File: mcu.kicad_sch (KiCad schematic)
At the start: 41 parts, among them SW1 SW_Nidec_CAS-120A1, SW2 CK_KMS2xxG, U1 STM32U5G9ZJTxQ, Y1 NX2016SA-16MHZ-EXS00A-CS07826, Y2 NX2012SA-32.768K-STD-MUB-1

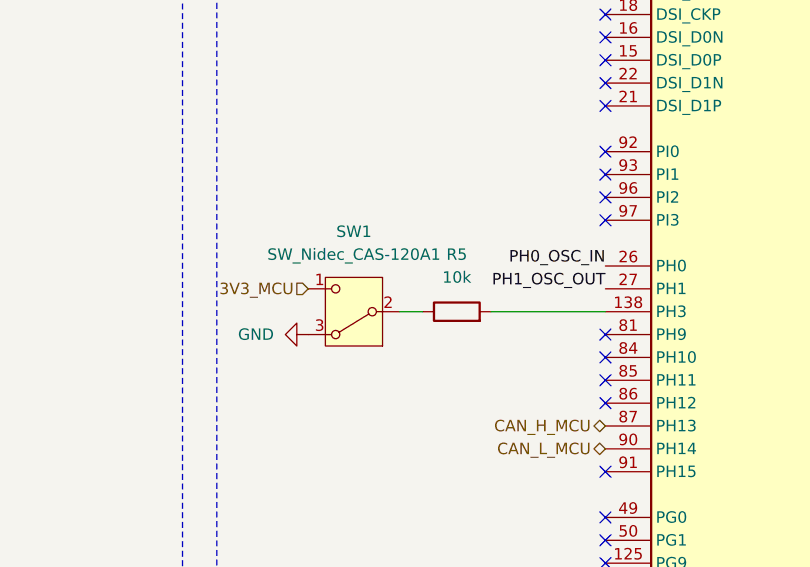
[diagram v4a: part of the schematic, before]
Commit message: Add switch reference form WE for boot selection mode
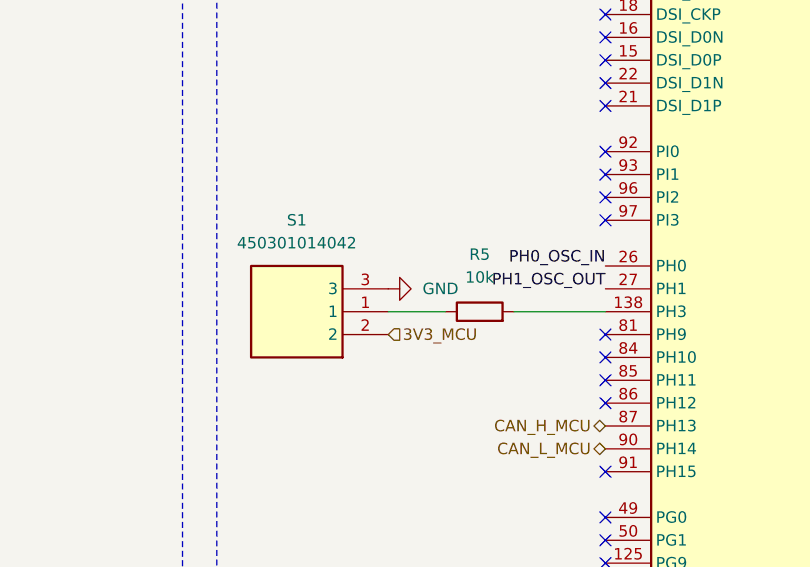
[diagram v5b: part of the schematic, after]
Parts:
- removed SW1: SW_Nidec_CAS-120A1, Button_Switch_SMD:Nidec_Copal_CAS-120A, symbol Switch:SW_Nidec_CAS-120A1
- added S1: 450301014042, weather-station-poc-fp:450301014042, symbol weather-station-poc-sym:450301014042
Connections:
- net 3V3_MCU: now also S1.2
- net GND: now also S1.3
- net at R5.1: now also S1.1
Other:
- moved on the sheet: R5
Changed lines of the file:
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@@
 	(wire
 		(pts
-			(xy 226.06 110.49) (xy 238.76 110.49)
+			(xy 228.6 110.49) (xy 238.76 110.49)
 		)
 		(stroke
@@
 	(wire
 		(pts
-			(xy 276.86 232.41) (xy 279.4 232.41)
+			(xy 220.98 110.49) (xy 214.63 110.49)
 		)
 		(stroke
@@
 	(wire
 		(pts
-			(xy 341.63 157.48) (xy 341.63 153.67)
+			(xy 276.86 232.41) (xy 279.4 232.41)
 		)
 		(stroke
@@
 	(wire
 		(pts
-			(xy 215.9 110.49) (xy 218.44 110.49)
+			(xy 341.63 157.48) (xy 341.63 153.67)
 		)
 		(stroke
@@
 	(hierarchical_label "3V3_MCU"
 		(shape input)
-		(at 205.74 107.95 180)
+		(at 214.63 113.03 0)
 		(effects
 			(font
 				(size 1.27 1.27)
 			)
-			(justify right)
+			(justify left)
 		)
 	)
@@
 	)
 	(symbol
-		(lib_id "power:GND")
-		(at 205.74 113.03 270)
-		(unit 1)
-		(exclude_from_sim no)
-		(in_bom yes)
-		(on_board yes)
-		(dnp no)
-		(fields_autoplaced yes)
-		(property "Reference" "#PWR054"
-			(at 199.39 113.03 0)
-			(effects
-				(font
-					(size 1.27 1.27)
-				)
-				(hide yes)
-			)
-		)
-		(property "Value" "GND"
-			(at 201.93 113.0299 90)
-			(effects
-				(font
-					(size 1.27 1.27)
-				)
-				(justify right)
-			)
-		)
-		(property "Footprint" ""
-			(at 205.74 113.03 0)
-			(effects
-				(font
-					(size 1.27 1.27)
-				)
-				(hide yes)
-			)
-		)
-		(property "Datasheet" ""
-			(at 205.74 113.03 0)
-			(effects
-				(font
-					(size 1.27 1.27)
-				)
-				(hide yes)
-			)
-		)
-		(property "Description" "Power symbol creates a global label with name \"GND\" , ground"
-			(at 205.74 113.03 0)
-			(effects
-				(font
-					(size 1.27 1.27)
-				)
-				(hide yes)
-			)
-		)
-		(pin "1"
-		)
-		(instances
-			(project "weather-station-poc"
-				(path "/38eb53bb-294e-46e4-ad59-fd355ca373b9/5f00b1ab-9f48-4782-8810-a8d68b4e6a2f"
-					(reference "#PWR054")
-					(unit 1)
-				)
-			)
-		)
-	)
-	(symbol
 		(lib_id "Device:C")
 		(at 81.28 90.17 0)
@@
 	(symbol
 		(lib_id "Device:R")
-		(at 222.25 110.49 90)
+		(at 224.79 110.49 90)
 		(unit 1)
 		(exclude_from_sim no)
@@
 		(fields_autoplaced yes)
 		(property "Reference" "R5"
-			(at 222.25 104.14 90)
+			(at 224.79 104.14 90)
 			(effects
 				(font
@@
 		)
 		(property "Value" "10k"
-			(at 222.25 106.68 90)
+			(at 224.79 106.68 90)
 			(effects
 				(font
@@
 		)
 		(property "Footprint" "Resistor_SMD:R_0603_1608Metric_Pad0.98x0.95mm_HandSolder"
-			(at 222.25 112.268 90)
+			(at 224.79 112.268 90)
 			(effects
 				(font
@@
 		)
 		(property "Datasheet" "~"
-			(at 222.25 110.49 0)
+			(at 224.79 110.49 0)
 			(effects
 				(font
@@
 		)
 		(property "Description" "Resistor"
-			(at 222.25 110.49 0)
+			(at 224.79 110.49 0)
 			(effects
 				(font
@@
 	)
 	(symbol
+		(lib_id "weather-station-poc-sym:450301014042")
+		(at 214.63 113.03 180)
+		(unit 1)
+		(exclude_from_sim no)
+		(in_bom yes)
+		(on_board yes)
+		(dnp no)
+		(fields_autoplaced yes)
+		(property "Reference" "S1"
+			(at 204.47 100.33 0)
+			(effects
+				(font
+					(size 1.27 1.27)
+				)
+			)
+		)
+		(property "Value" "450301014042"
+			(at 204.47 102.87 0)
+			(effects
+				(font
+					(size 1.27 1.27)
+				)
+			)
+		)
+		(property "Footprint" "weather-station-poc-fp:450301014042"
+			(at 198.12 18.11 0)
+			(effects
+				(font
+					(size 1.27 1.27)
+				)
+				(justify left top)
+				(hide yes)
+			)
+		)
+		(property "Datasheet" "https://www.we-online.com/catalog/datasheet/450301014042.pdf"
+			(at 198.12 -81.89 0)
+			(effects
+				(font
+					(size 1.27 1.27)
+				)
+				(justify left top)
+				(hide yes)
+			)
+		)
+		(property "Description" "WS-SLTV Mini Slide Switch 10mm*2.5mm. SPDT, ON-ON, 2.54mm, vertical type, THT, bulk"
+			(at 214.63 113.03 0)
+			(effects
+				(font
+					(size 1.27 1.27)
+				)
+				(hide yes)
+			)
+		)
+		(property "Height" ""
+			(at 198.12 -281.89 0)
+			(effects
+				(font
+					(size 1.27 1.27)
+				)
+				(justify left top)
+				(hide yes)
+			)
+		)
+		(property "Mouser Part Number" "710-450301014042"
+			(at 198.12 -381.89 0)
+			(effects
+				(font
+					(size 1.27 1.27)
+				)
+				(justify left top)
+				(hide yes)
+			)
+		)
+		(property "Mouser Price/Stock" "https://www.mouser.co.uk/ProductDetail/Wurth-Elektronik/450301014042?qs=wr8lucFkNMW0uepaR4R%2Fww%3D%3D"
+			(at 198.12 -481.89 0)
+			(effects
+				(font
+					(size 1.27 1.27)
+				)
+				(justify left top)
+				(hide yes)
+			)
+		)
+		(property "Manufacturer_Name" "Wurth Elektronik"
+			(at 198.12 -581.89 0)
+			(effects
+				(font
+					(size 1.27 1.27)
+				)
+				(justify left top)
+				(hide yes)
+			)
+		)
+		(property "Manufacturer_Part_Number" "450301014042"
+			(at 198.12 -681.89 0)
+			(effects
+				(font
+					(size 1.27 1.27)
+				)
+				(justify left top)
+				(hide yes)
+			)
+		)
+		(pin "2"
+		)
+		(pin "3"
+		)
+		(pin "1"
+		)
+		(instances
+			(project ""
+				(path "/38eb53bb-294e-46e4-ad59-fd355ca373b9/5f00b1ab-9f48-4782-8810-a8d68b4e6a2f"
+					(reference "S1")
+					(unit 1)
+				)
+			)
+		)
+	)
+	(symbol
 		(lib_id "Device:C")
 		(at 132.08 179.07 0)
@@
 	(symbol
 		(lib_id "power:GND")
+		(at 214.63 107.95 90)
+		(unit 1)
+		(exclude_from_sim no)
+		(in_bom yes)
+		(on_board yes)
+		(dnp no)
+		(fields_autoplaced yes)
+		(property "Reference" "#PWR0122"
+			(at 220.98 107.95 0)
+			(effects
+				(font
+					(size 1.27 1.27)
+				)
+				(hide yes)
+			)
+		)
+		(property "Value" "GND"
+			(at 218.44 107.9499 90)
+			(effects
+				(font
+					(size 1.27 1.27)
+				)
+				(justify right)
+			)
+		)
+		(property "Footprint" ""
+			(at 214.63 107.95 0)
+			(effects
+				(font
+					(size 1.27 1.27)
+				)
+				(hide yes)
+			)
+		)
+		(property "Datasheet" ""
+			(at 214.63 107.95 0)
+			(effects
+				(font
+					(size 1.27 1.27)
+				)
+				(hide yes)
+			)
+		)
+		(property "Description" "Power symbol creates a global label with name \"GND\" , ground"
+			(at 214.63 107.95 0)
+			(effects
+				(font
+					(size 1.27 1.27)
+				)
+				(hide yes)
+			)
+		)
+		(pin "1"
+		)
+		(instances
+			(project "weather-station-poc"
+				(path "/38eb53bb-294e-46e4-ad59-fd355ca373b9/5f00b1ab-9f48-4782-8810-a8d68b4e6a2f"
+					(reference "#PWR0122")
+					(unit 1)
+				)
+			)
+		)
+	)
+	(symbol
+		(lib_id "power:GND")
 		(at 100.33 207.01 0)
 		(unit 1)
@@
 					(unit 1)
 				)
-			)
-		)
-	)
-	(symbol
-		(lib_id "Switch:SW_Nidec_CAS-120A1")
-		(at 210.82 110.49 180)
-		(unit 1)
-		(exclude_from_sim no)
-		(in_bom yes)
-		(on_board yes)
-		(dnp no)
-		(fields_autoplaced yes)
-		(property "Reference" "SW1"
-			(at 210.82 101.6 0)
-			(effects
-				(font
-					(size 1.27 1.27)
-				)
-			)
-		)
-		(property "Value" "SW_Nidec_CAS-120A1"
-			(at 210.82 104.14 0)
-			(effects
-				(font
-					(size 1.27 1.27)
-				)
-			)
-		)
-		(property "Footprint" "Button_Switch_SMD:Nidec_Copal_CAS-120A"
-			(at 210.82 100.33 0)
-			(effects
-				(font
-					(size 1.27 1.27)
-				)
-				(hide yes)
-			)
-		)
-		(property "Datasheet" "https://www.nidec-components.com/e/catalog/switch/cas.pdf"
-			(at 210.82 102.87 0)
-			(effects
-				(font
-					(size 1.27 1.27)
-				)
-				(hide yes)
-			)
-		)
-		(property "Description" "Switch, single pole double throw"
-			(at 210.82 110.49 0)
-			(effects
-				(font
-					(size 1.27 1.27)
-				)
-				(hide yes)
-			)
-		)
-		(pin "2"
-		)
-		(pin "1"
-		)
-		(pin "3"
-		)
-		(instances
-			(project ""
-				(path "/38eb53bb-294e-46e4-ad59-fd355ca373b9/5f00b1ab-9f48-4782-8810-a8d68b4e6a2f"
-					(reference "SW1")
-					(unit 1)
-				)

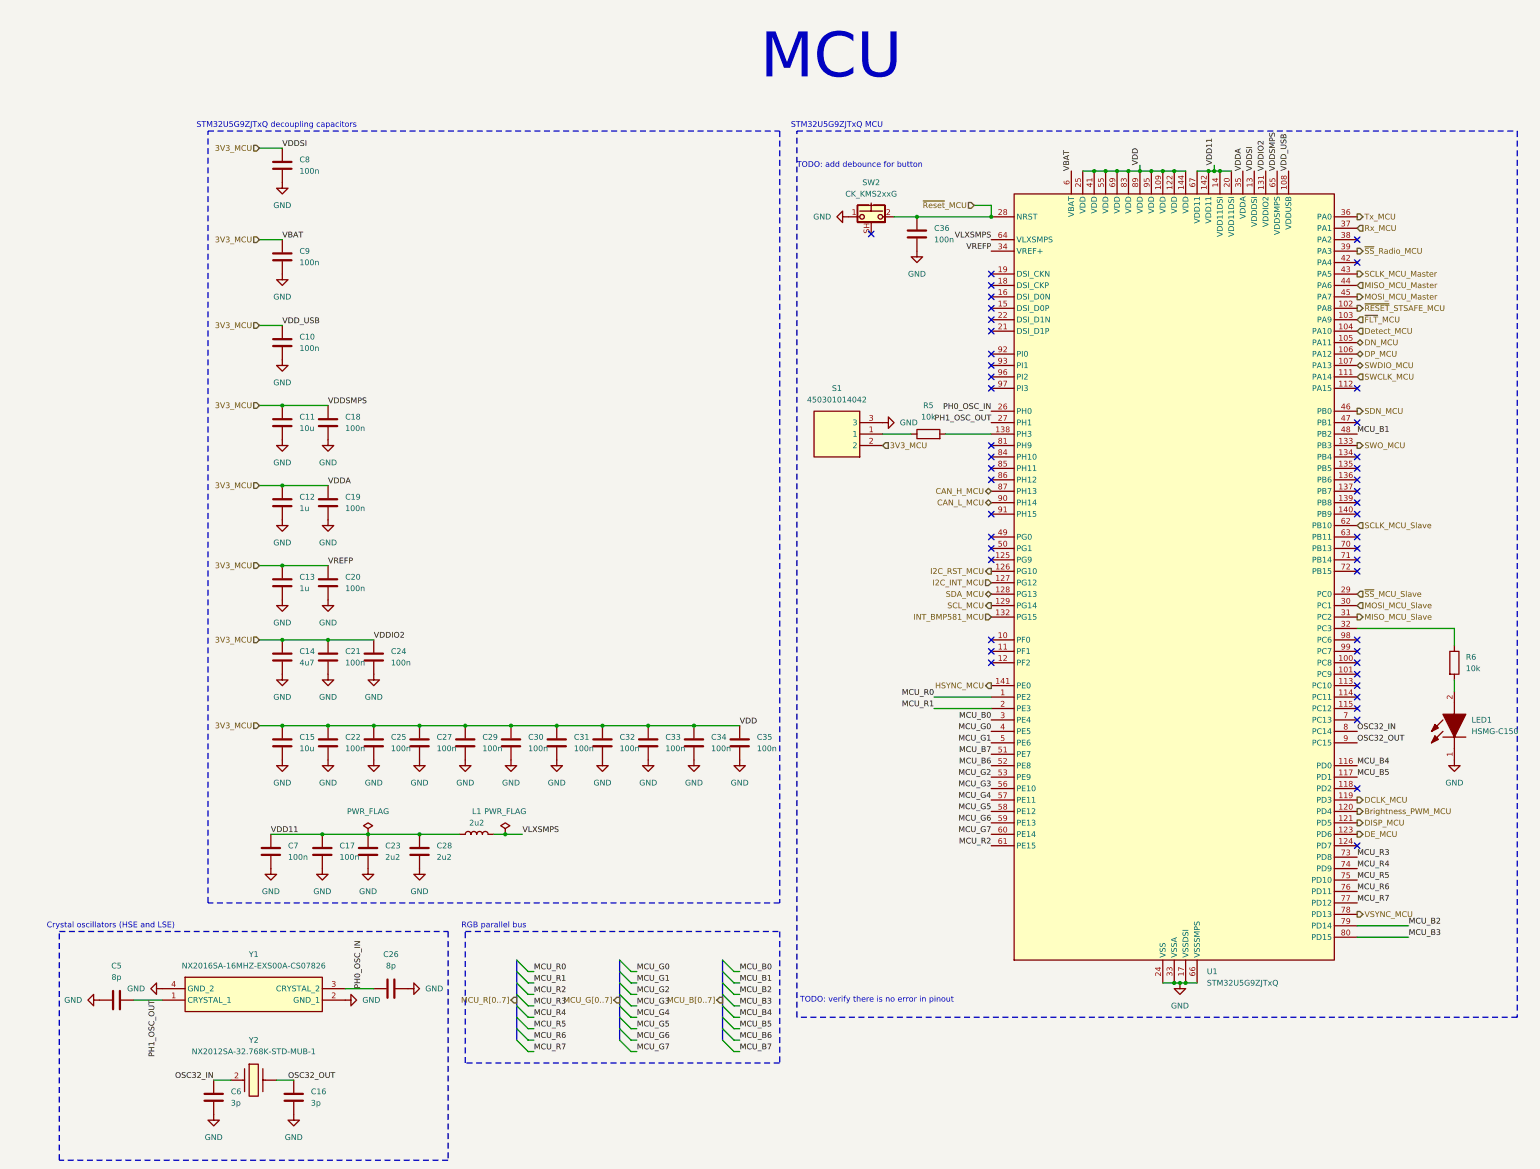
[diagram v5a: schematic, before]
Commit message: Add a button reference for reset MCU
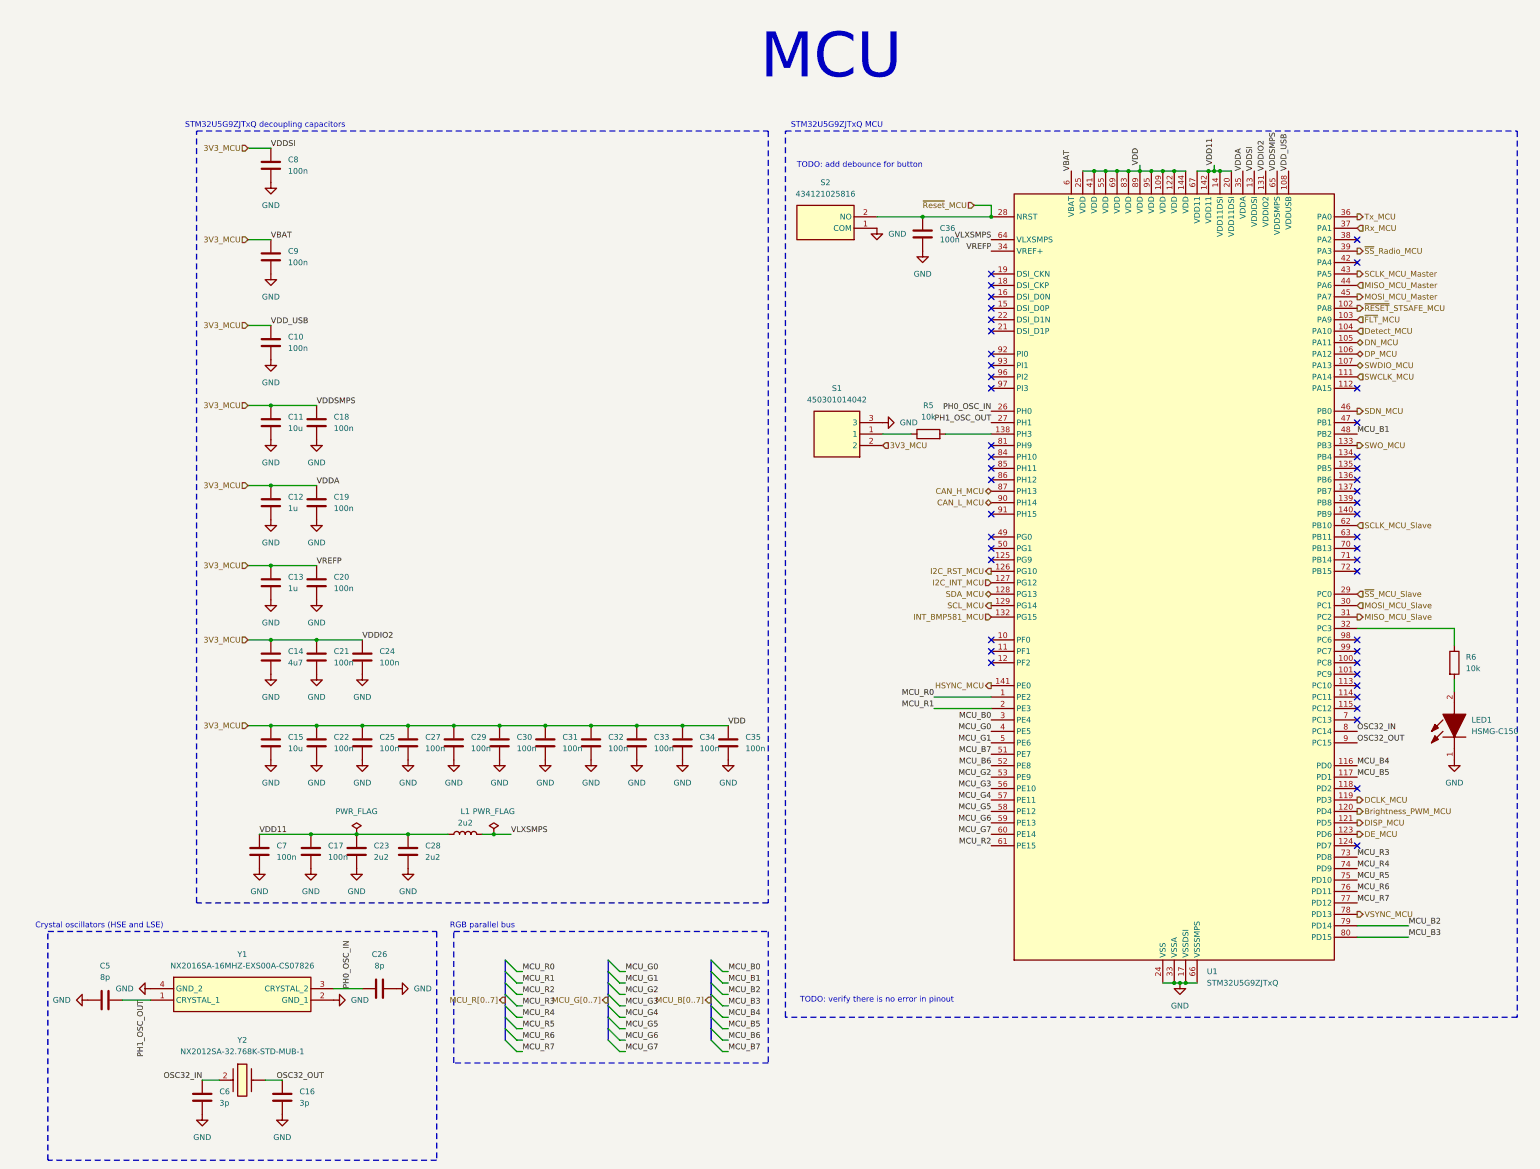
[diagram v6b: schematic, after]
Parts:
- removed SW2: CK_KMS2xxG, Button_Switch_SMD:SW_SPST_CK_KMS2xxGP, symbol Switch:CK_KMS2xxG
- added S2: 434121025816, weather-station-poc-fp:434121050816, symbol weather-station-poc-sym:434121025816
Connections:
- net GND: now also S2.1 (COM)
- net ~{Reset}_MCU: now also S2.2 (NO)
- no-connect marks 46 -> 45
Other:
- moved on the sheet: C10, C11, C12, C13, C14, C15, C16, C17, C18, C19, C20, C21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

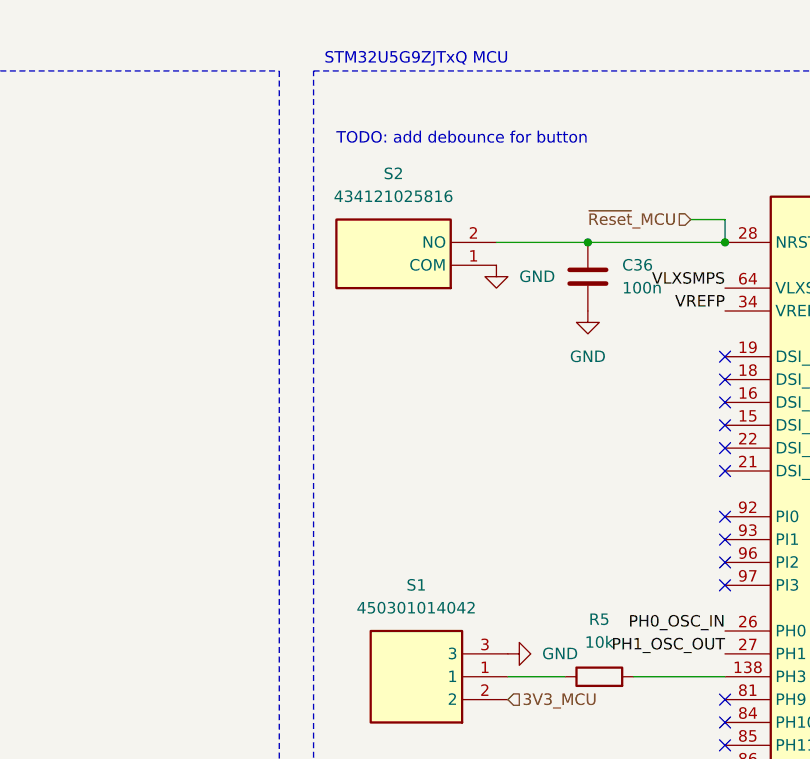
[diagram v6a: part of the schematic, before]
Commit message: Use preconised diodes for USB-C by ST
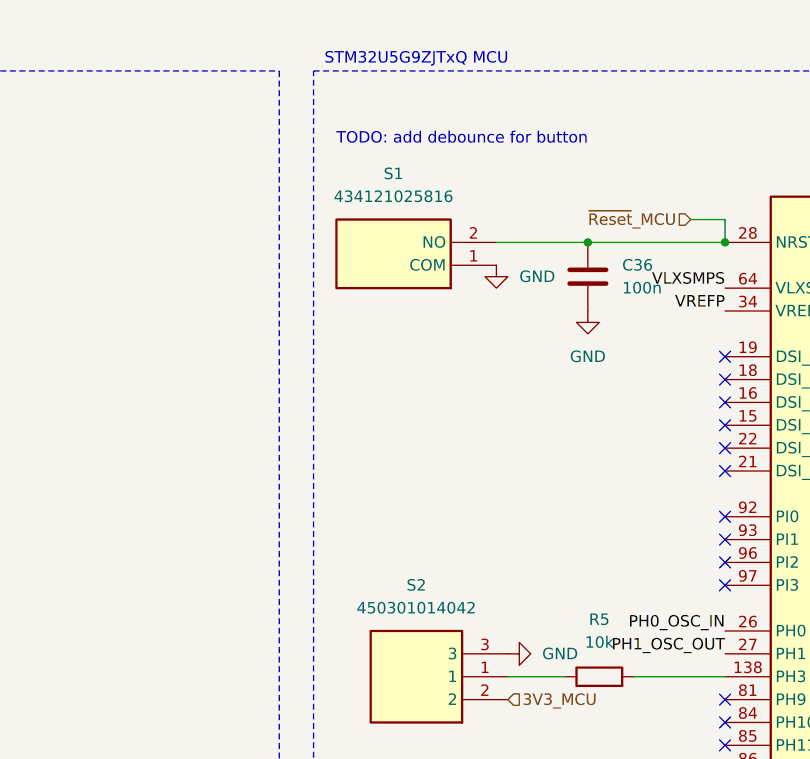
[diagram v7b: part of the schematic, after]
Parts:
- renumbered S2 to S1, S1 to S2
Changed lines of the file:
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@@
 		(dnp no)
 		(fields_autoplaced yes)
-		(property "Reference" "S2"
+		(property "Reference" "S1"
 			(at 201.93 54.61 0)
 			(effects
@@
 			(project ""
 				(path "/38eb53bb-294e-46e4-ad59-fd355ca373b9/5f00b1ab-9f48-4782-8810-a8d68b4e6a2f"
-					(reference "S2")
+					(reference "S1")
 					(unit 1)
 				)
@@
 		(dnp no)
 		(fields_autoplaced yes)
-		(property "Reference" "S1"
+		(property "Reference" "S2"
 			(at 204.47 100.33 0)
 			(effects
@@
 			(project ""
 				(path "/38eb53bb-294e-46e4-ad59-fd355ca373b9/5f00b1ab-9f48-4782-8810-a8d68b4e6a2f"
-					(reference "S1")
+					(reference "S2")
 					(unit 1)
 				)
@@
 		(dnp no)
 		(fields_autoplaced yes)
-		(property "Reference" "#PWR055"
+		(property "Reference" "#PWR054"
 			(at 213.36 71.12 0)
 			(effects
@@
 			(project "weather-station-poc"
 				(path "/38eb53bb-294e-46e4-ad59-fd355ca373b9/5f00b1ab-9f48-4782-8810-a8d68b4e6a2f"
-					(reference "#PWR055")
+					(reference "#PWR054")
 					(unit 1)
 				)
@@
 		(dnp no)
 		(fields_autoplaced yes)
-		(property "Reference" "#PWR0122"
+		(property "Reference" "#PWR055"
 			(at 220.98 107.95 0)
 			(effects
@@
 			(project "weather-station-poc"
 				(path "/38eb53bb-294e-46e4-ad59-fd355ca373b9/5f00b1ab-9f48-4782-8810-a8d68b4e6a2f"
-					(reference "#PWR0122")
-					(unit 1)
-				)
+					(reference "#PWR055")
+					(unit 1)
+				)
